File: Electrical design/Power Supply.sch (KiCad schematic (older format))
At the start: 23 parts, among them Q301 Q_PMOS_GSD, Q302 Q_NMOS_GSD, U301 NCV551SN33T1G, U302 MAX6070

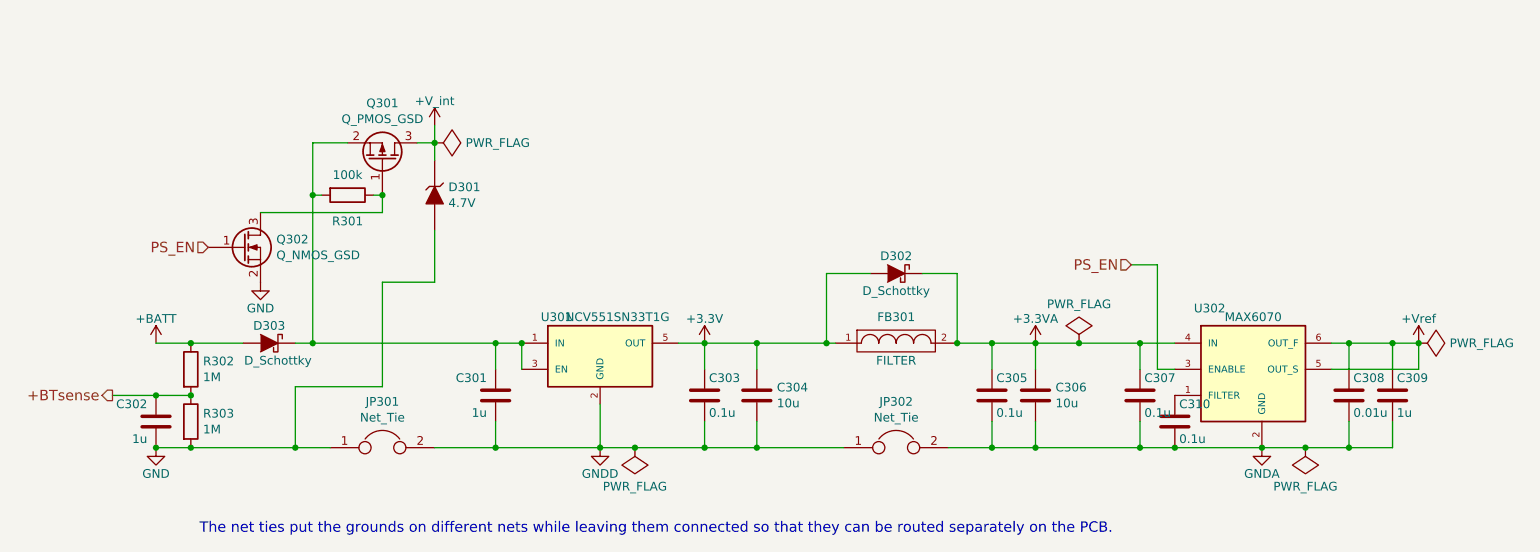
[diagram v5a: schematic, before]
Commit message: Add documentation. Fix some issues found while writing it.
The issues fixed:
Change R245-246 to 1M.
Remove D211-212 and add D213-214.
Power the analog switches from +V_int.
Reconfigure range combination jumpers.
Remove "GND" net.
Correct values of C103-105, and add R106-108 (correcting values of R101-103).
Change +V_int around to be based of +3.3VA instead of +BATT, and clamp to 3.5 V.
Along with above, remove GND rail, mostly replacing with GNDA.
Update PCB for changes.
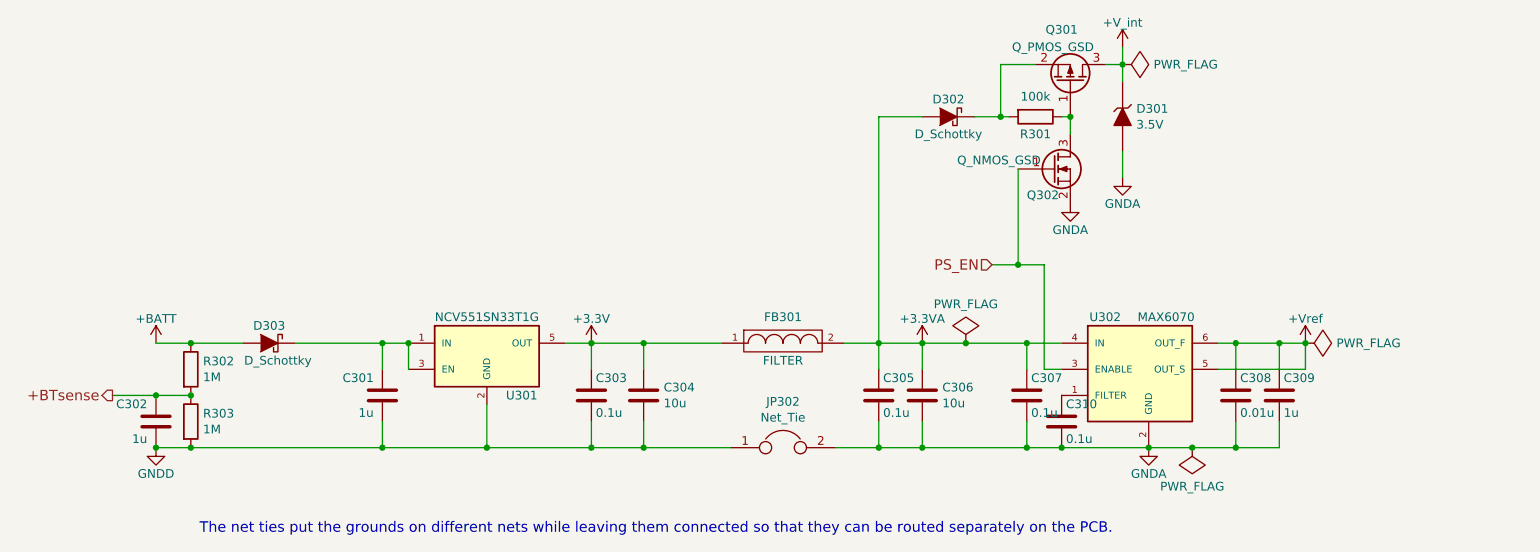
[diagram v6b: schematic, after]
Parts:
- removed JP301: Net_Tie, my footprints:Net_Tie, symbol JUMPER
- D301: value 4.7V -> 3.5V
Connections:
- net +3.3VA: now also D302.2 (A); no longer D302.1 (K)
- net +3V3: no longer D302.2 (A)
- net GNDA: now also D301.1 (A), Q302.2 (S)
- net GNDD: now also C302.2, R303.2
- net at C301.1, D303.1 (K), U301.1 (IN)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: no longer Q301.2 (S), R301.2
- removed net GND: C302.2, D301.1 (A), Q302.2 (S), R303.2
- new net: D302.1 (K), Q301.2 (S), R301.2
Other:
- moved on the sheet: C301, C303, C304, C305, C306, C307, C308, C309, C310, D301, D302, FB301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

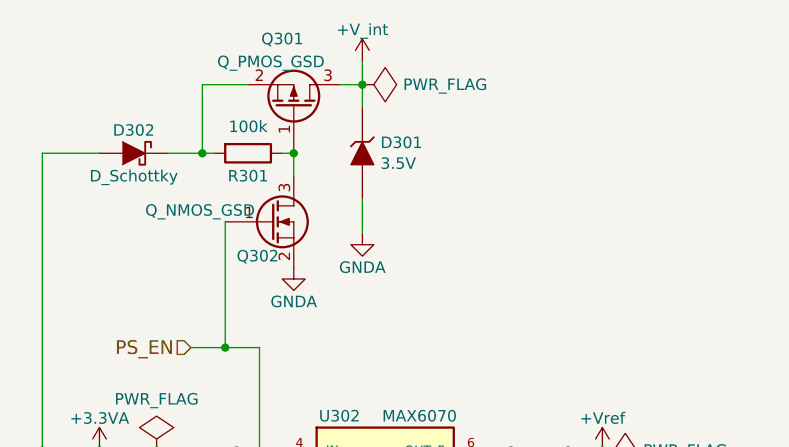
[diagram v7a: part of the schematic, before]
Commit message: Fix current circuit connection, PCB layout.
The current measurement circuit has to connect directly to the Common terminal!
The PCB layout had traces going between the pads of the Common terminal, where
there's actually a non-plated hole. I've updated the footprint to include the hole,
although unfortunately that produces about 20 DRC errors, and also re-routed stuff.
Also updated the value of D301 to match a real Zener diode.
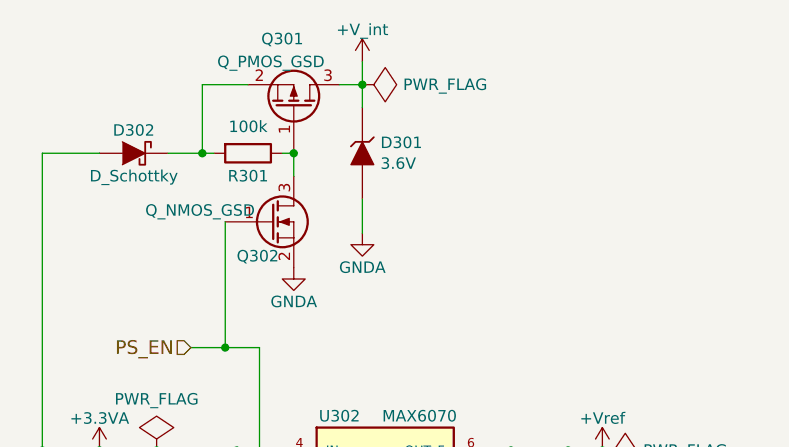
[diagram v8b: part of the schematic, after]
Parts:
- D301: value 3.5V -> 3.6V
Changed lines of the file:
@@
 P 7850 2050
 F 0 "D301" V 7804 2129 50  0000 L CNN
-F 1 "3.5V" V 7895 2129 50  0000 L CNN
+F 1 "3.6V" V 7895 2129 50  0000 L CNN
 F 2 "TO_SOT_Packages_SMD:SOT-23" H 7850 2050 50  0001 C CNN
 F 3 "" H 7850 2050 50  0000 C CNN
